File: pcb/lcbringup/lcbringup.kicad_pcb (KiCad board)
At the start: 4 copper layers, 80.8 x 69 mm, 189 parts, among them J1 XILINX_JTAG, J10 SMPM, J11 ARF6-08-S-D-A-K-TR, J12 SMPM, J13 SMPM, J14 SMPM, J15 SMPM, J16 SMPM, J17 SMPM, J18 SMPM, J19 SMPM, J2 CONN_01X10, J20 SMPM, J21 SMPM, J22 SMPM, J23 CONN_IBC_MGMT_HOST, J3 CONN_SFP_HOST, J4 CORTEX_DEBUG_ETM, J5 CONN_01X03, J7 SFP_CAGE, J8 CONN_IBC_MGMT, J9 CONN_ATX12V, M1 SCREWHOLE, M2 SCREWHOLE, M3 SCREWHOLE, M4 SCREWHOLE, U1 XC7A35T-2FGG484C, U10 MUN12AD03-SE, U11 MUN12AD03-SE, U2 STM32H735-UFBGA176-25, U3 ECS-1612MV-250-CN, U4 ECS-1612MV-250-CN, U5 MUN12AD03-SE, U7 AT24MAC402, U8 SIT9121AI-2BF-XXS156.250000G, U9 MUN12AD03-SE

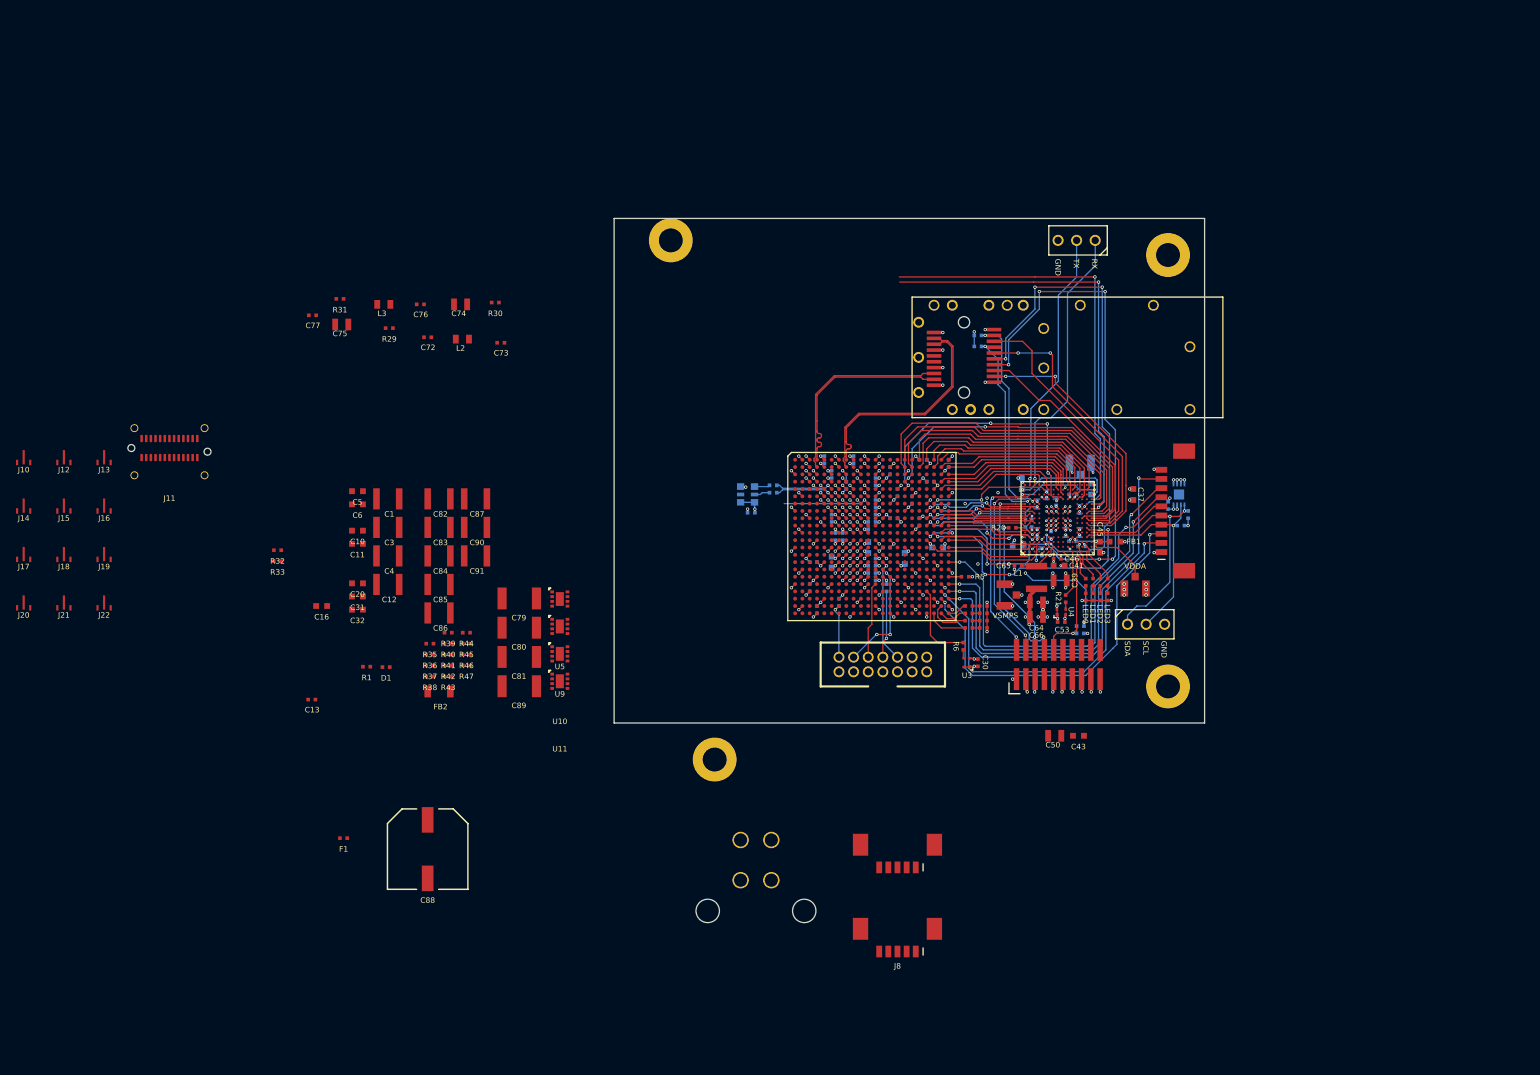
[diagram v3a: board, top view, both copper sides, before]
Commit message: Continued lcbringup layout on ARF6 area
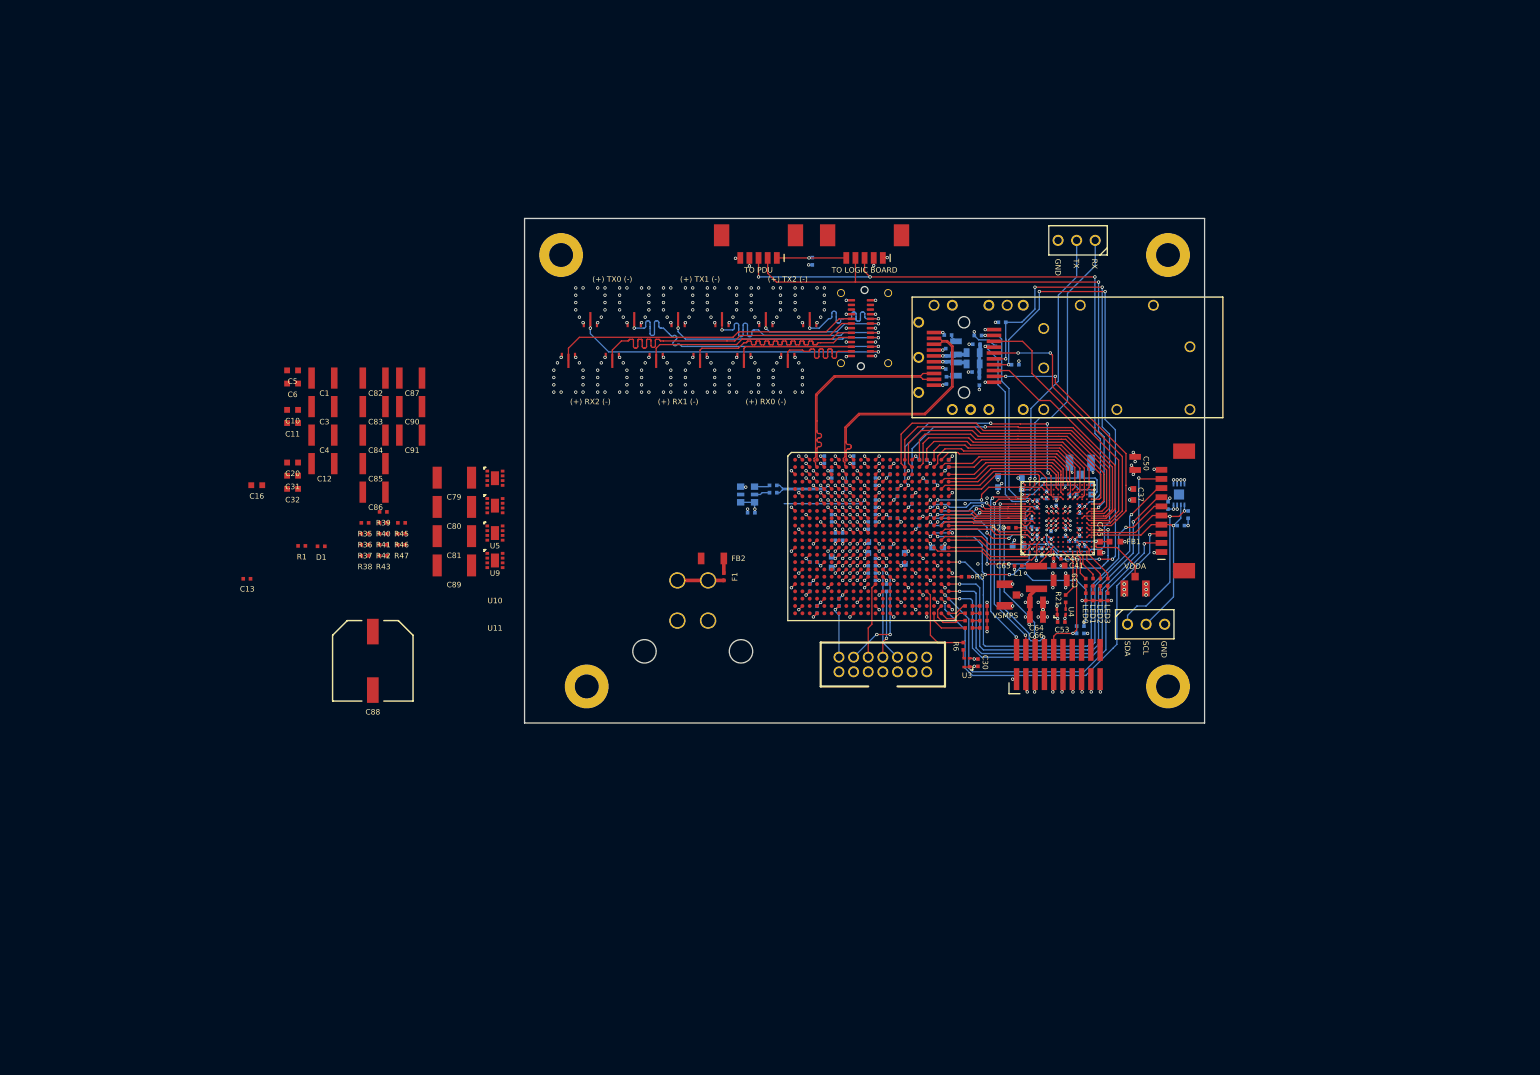
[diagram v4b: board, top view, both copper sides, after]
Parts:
- C43, C72, C73, C74, C75, C76, C77, L2, L3, R29, R30, R31, R32, R33, R44: moved to B.Cu
- moved J17 106.8 mm to (71.0, 45.8), turned to 180 degrees
- moved R33 104.3 mm to (100.3, 38.2), turned to 180 degrees
- moved R32 104.0 mm to (102.1, 44.0)
- moved J16 99.8 mm to (74.0, 35.5)
- moved J15 99.3 mm to (68.0, 35.5)
- moved J14 98.8 mm to (62.0, 35.5)
- moved J8 96.7 mm to (67.0, 29.4)
- moved J11 96.0 mm to (81.0, 39.0), turned to 90 degrees
- moved J18 95.5 mm to (65.0, 45.8), turned to 180 degrees
- moved J20 91.1 mm to (53.0, 45.8), turned to 180 degrees
- moved C77 86.9 mm to (92.6, 44.1), turned to -90 degrees
- moved J19 84.4 mm to (59.0, 45.8), turned to 180 degrees
- moved C75 84.2 mm to (94.0, 44.6), turned to -90 degrees
- moved R31 83.7 mm to (92.7, 46.1), turned to 90 degrees
- moved J23 83.5 mm to (81.5, 29.4)
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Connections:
- J10 pad 2: /ARF6 breakout/GND -> /GND
- J11 pad 1: /ARF6 breakout/GND -> /GND
- J11 pad 13: /ARF6 breakout/GND -> /GND
- J11 pad 14: /ARF6 breakout/GND -> /GND
- J11 pad 19: /ARF6 breakout/GND -> /GND
- J11 pad 2: /ARF6 breakout/GND -> /GND
- J11 pad 20: /ARF6 breakout/GND -> /GND
- J11 pad 25: /ARF6 breakout/GND -> /GND
- J11 pad 26: /ARF6 breakout/GND -> /GND
- J11 pad 27: /ARF6 breakout/GND -> /GND
- J11 pad 7: /ARF6 breakout/GND -> /GND
- J11 pad 8: /ARF6 breakout/GND -> /GND
- J12 pad 2: /ARF6 breakout/GND -> /GND
- J13 pad 2: /ARF6 breakout/GND -> /GND
- J14 pad 2: /ARF6 breakout/GND -> /GND
- J15 pad 2: /ARF6 breakout/GND -> /GND
- J16 pad 2: /ARF6 breakout/GND -> /GND
- J17 pad 2: /ARF6 breakout/GND -> /GND
- J18 pad 2: /ARF6 breakout/GND -> /GND
- J19 pad 2: /ARF6 breakout/GND -> /GND
- J20 pad 2: /ARF6 breakout/GND -> /GND
- J21 pad 2: /ARF6 breakout/GND -> /GND
- J22 pad 2: /ARF6 breakout/GND -> /GND
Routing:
- net /GND: track 745.1 -> 1065.3 mm, vias 195 -> 380
- net /3V3_SB: track 19.2 -> 140.8 mm, vias 4 -> 7
- net /ARF6 breakout/QSGMII_TX0_P: track 0.00 -> 43.5 mm, vias 0 -> 2
- net /ARF6 breakout/QSGMII_TX0_N: track 0.00 -> 43.4 mm, vias 0 -> 2
- net /ARF6 breakout/QSGMII_RX2_N: track 0.00 -> 42.1 mm
- net /ARF6 breakout/QSGMII_RX2_P: track 0.00 -> 42.0 mm
- net /ARF6 breakout/QSGMII_TX1_P: track 0.00 -> 30.7 mm, vias 0 -> 2
- net /ARF6 breakout/QSGMII_TX1_N: track 0.00 -> 30.6 mm, vias 0 -> 2
- net /ARF6 breakout/QSGMII_RX1_N: track 0.00 -> 29.3 mm
- net /ARF6 breakout/QSGMII_RX1_P: track 0.00 -> 29.1 mm
- net /3V3: track 326.1 -> 352.2 mm, vias 71 -> 77
- net /Power supply/SUPER_I2C_SDA: track 60.1 -> 84.9 mm, vias 2 -> 4
- net /Power supply/SUPER_I2C_SCL: track 59.7 -> 83.6 mm
- net /ARF6 breakout/QSGMII_TX2_P: track 0.00 -> 18.4 mm, vias 0 -> 2
- net /ARF6 breakout/QSGMII_TX2_N: track 0.00 -> 18.3 mm, vias 0 -> 2
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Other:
- board size 80.8 x 69 mm -> 93 x 69 mm
- board text added: "(+) RX0 (-)"
- board text added: "(+) RX1 (-)"
- board text added: "(+) RX2 (-)"
- board text added: "(+) TX0 (-)"
- board text added: "(+) TX1 (-)"
- board text added: "(+) TX2 (-)"
- board text added: "TO LOGIC BOARD"
- board text added: "TO PDU"

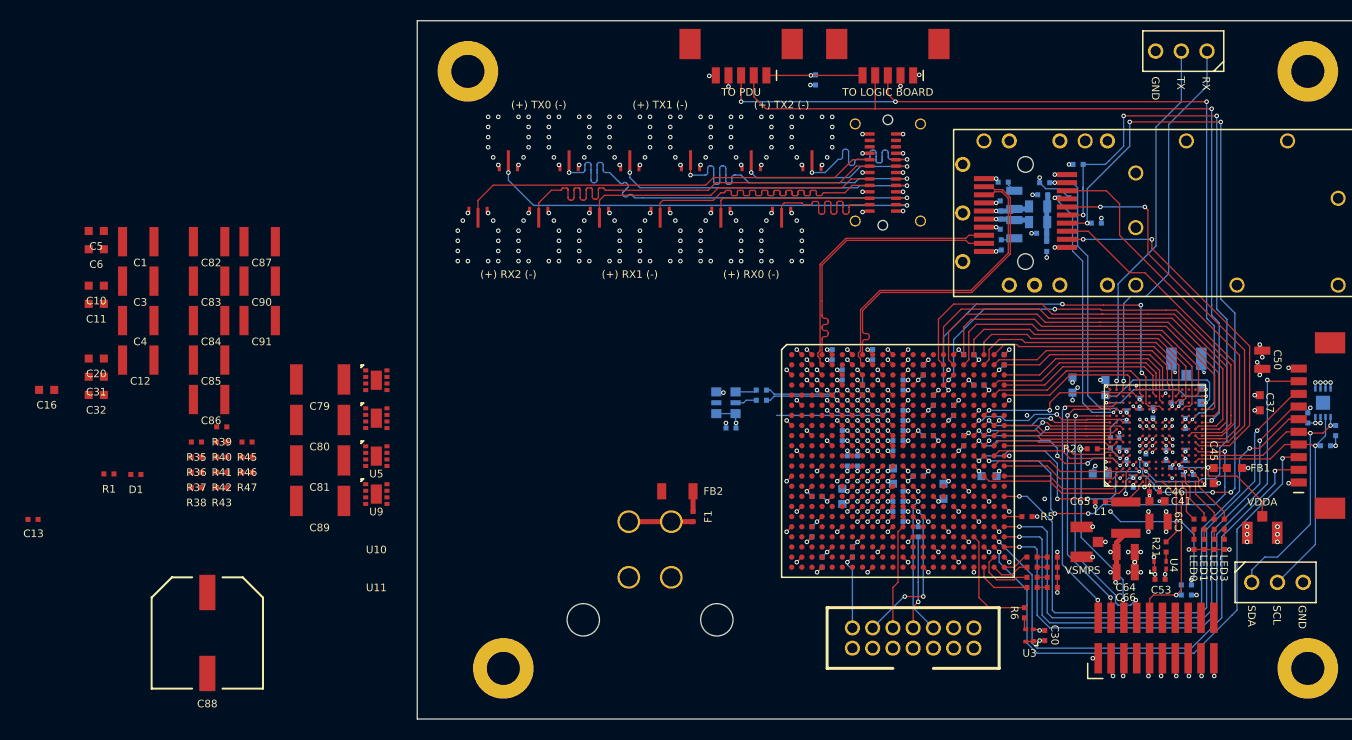
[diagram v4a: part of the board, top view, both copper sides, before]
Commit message: Conitnued lcbringup layout, power supply is now floorplanned
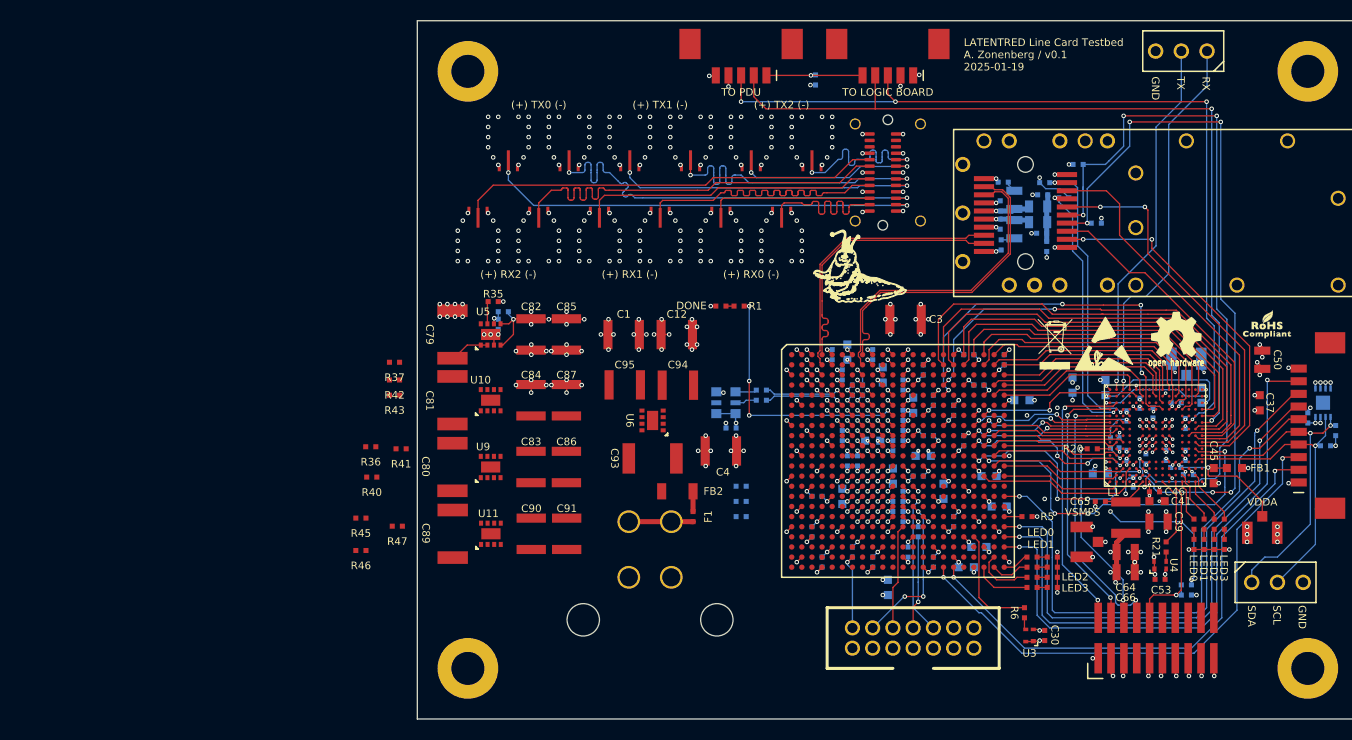
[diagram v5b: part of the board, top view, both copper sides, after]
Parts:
- removed C88: DNP, azonenberg_pcb:CAP_AL_10MM_SMT
- added C100: 0.47 uF, azonenberg_pcb:EIA_0402_CAP_NOSILK, B.Cu at (86.0, 77.5)
- added C101: 0.47 uF, azonenberg_pcb:EIA_0402_CAP_NOSILK, B.Cu at (88.0, 73.5)
- added C93: 22 uF, azonenberg_pcb:EIA_1812_CAP_NOSILK, F.Cu at (58.2, 67.2)
- added C94: 22 uF, azonenberg_pcb:EIA_1210_CAP_NOSILK, F.Cu at (60.8, 60.0)
- added C95: 22 uF, azonenberg_pcb:EIA_1210_CAP_NOSILK, F.Cu at (55.5, 60.0)
- added C96: 4.7 uF, azonenberg_pcb:EIA_0603_CAP_NOSILK, B.Cu at (89.2, 78.0)
- added C97: 4.7 uF, azonenberg_pcb:EIA_0603_CAP_NOSILK, B.Cu at (81.5, 80.0)
- added C98: 0.47 uF, azonenberg_pcb:EIA_0402_CAP_NOSILK, B.Cu at (80.0, 77.5)
- added C99: 0.47 uF, azonenberg_pcb:EIA_0402_CAP_NOSILK, B.Cu at (83.5, 76.5)
- added M5: MECHANICAL, azonenberg_pcb:LONGTHING-1200DPI, F.Cu at (79.3, 48.6)
- added M6: MECHANICAL, azonenberg_pcb:LOGO_ESD_SENSITIVE_7MM, F.Cu at (103.0, 56.0)
- added M7: MECHANICAL, w_logo:Logo_silk_OSHW_6x6mm, F.Cu at (110.0, 55.0)
- added M8: MECHANICAL, w_logo:Logo_silk_ROHS_5x2.8mm, F.Cu at (119.0, 54.0)
- added M9: MECHANICAL, w_logo:Logo_silk_WEEE_3.4x5mm, F.Cu at (98.0, 56.0)
- added R12: 10K, azonenberg_pcb:EIA_0402_RES_NOSILK, B.Cu at (67.0, 70.0)
- added R13: FIXME, azonenberg_pcb:EIA_0402_RES_NOSILK, B.Cu at (67.0, 71.5)
- added R14: FIXME, azonenberg_pcb:EIA_0402_RES_NOSILK, B.Cu at (67.0, 73.0)
- added U6: MUN12AD03-SE, azonenberg_pcb:MODULE_CYNTEC_MUN12AD03-SE, F.Cu at (58.2, 63.5)
- C10, C11, C13, C16, C20, C31, C32, C5, C6, R38, R39: moved to B.Cu
- moved C20 91.6 mm to (94.8, 61.5)
- moved C32 89.9 mm to (92.5, 72.0), turned to 180 degrees
- moved C31 88.8 mm to (90.5, 76.0), turned to 180 degrees
- moved C16 86.9 mm to (85.0, 67.0)
- moved C13 82.0 mm to (78.0, 60.5), turned to 90 degrees
- moved C11 81.3 mm to (84.0, 62.0), turned to -90 degrees
- moved C5 79.0 mm to (81.0, 59.0), turned to 90 degrees
- moved C10 78.2 mm to (80.0, 65.5), turned to 180 degrees
- moved C3 75.9 mm to (83.2, 53.5)
- moved C6 74.9 mm to (77.5, 56.8), turned to 90 degrees
- moved R1 64.4 mm to (66.8, 52.2)
- moved D1 60.2 mm to (65.0, 52.2)
- moved C4 59.0 mm to (65.0, 66.5)
- moved C12 53.3 mm to (60.6, 55.0)
- moved C1 48.8 mm to (55.4, 55.0)
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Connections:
- U1 pad AA17: /3V3 -> /2V5
- U1 pad AB14: /3V3 -> /2V5
- U1 pad AB16: unconnected-(U1C-IO_L2P_T0_13-PadAB16) -> /MDIO and GPIO/MDIO
- U1 pad AB17: unconnected-(U1C-IO_L2N_T0_13-PadAB17) -> /MDIO and GPIO/MDC
- U1 pad V16: /3V3 -> /2V5
- U1 pad W13: /3V3 -> /2V5
- U1 pad W21: /MDIO and GPIO/MDC -> unconnected-(U1D-IO_L7P_T1_D09_14-PadW21)
- U1 pad Y10: /3V3 -> /2V5
- U1 pad Y21: /MDIO and GPIO/MDIO -> unconnected-(U1D-IO_L9P_T1_DQS_14-PadY21)
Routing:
- net /GND: track 1065.3 -> 1186.5 mm, vias 380 -> 421
- net /1V8: track 23.9 -> 97.6 mm, vias 7 -> 19
- net /1V0: track 56.3 -> 124.4 mm, vias 22 -> 38
- net /3V3: track 352.2 -> 409.3 mm
- net /2V5: track 0.00 -> 37.6 mm, vias 0 -> 6
- net Net-(U1A-DONE): track 11.9 -> 25.9 mm, vias 1 -> 4
- net /1V2: track 15.4 -> 22.4 mm
- net /Power supply/12V0: track 0.00 -> 3.99 mm
- net /Power supply/1V8_PGOOD: track 0.00 -> 2.23 mm
- net /Power supply/1V8_FB: track 0.00 -> 1.75 mm, vias 0 -> 1
- net /MDIO and GPIO/MDIO: track 52.3 -> 53.4 mm
- net Net-(D1-A): track 0.00 -> 0.80 mm
- net /MDIO and GPIO/MDC: track 51.3 -> 50.7 mm
- added copper zone on In1.Cu, net /GND
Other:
- board text added: "DONE"
- board text added: "LATENTRED Line Card Testbed A. Zonenberg / v0.1 2025-01-19"

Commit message: Finished initial lcbringup test board, ready for review
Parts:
- J5, TP1: footprint azonenberg_pcb:CONN_HEADER_2.54MM_1x3 -> azonenberg_pcb:CONN_HEADER_2.54MM_1x3_REFLOW
- R13: value FIXME -> 294K
- R14: value FIXME -> 93.1K
- R36, R37, R40, R41, R42, R43, R45, R46, R47: moved to B.Cu
- moved R46 14.5 mm to (43.6, 73.3), turned to 180 degrees
- moved R40 14.0 mm to (44.2, 66.1), turned to 180 degrees
- moved R14 13.9 mm to (58.0, 62.4), turned to 0 degrees
- moved R13 13.8 mm to (56.7, 62.3), turned to -90 degrees
- moved R12 12.9 mm to (55.7, 63.8)
- moved R45 12.5 mm to (41.9, 72.4), turned to 90 degrees
- moved R36 11.5 mm to (41.9, 65.6), turned to 90 degrees
- moved R42 11.0 mm to (43.7, 59.8), turned to 180 degrees
- moved R47 10.7 mm to (43.6, 72.5)
- moved R43 9.85 mm to (42.6, 61.0), turned to -90 degrees
- moved R41 9.63 mm to (43.0, 67.1), turned to -90 degrees
- moved R37 9.25 mm to (41.9, 59.1), turned to 90 degrees
- moved C40 0.10 mm to (112.5, 61.1)
- moved C80 0.10 mm to (38.5, 68.0), turned to 90 degrees
- moved C83 0.10 mm to (46.2, 68.0)
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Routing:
- net /GND: track 1186.5 -> 1343.5 mm, vias 421 -> 491
- net /3V3: track 409.3 -> 504.6 mm, vias 77 -> 87
- net /Power supply/12V0: track 3.99 -> 80.4 mm
- net /1V2: track 22.4 -> 70.2 mm, vias 6 -> 13
- net /2V5: track 37.6 -> 84.2 mm, vias 6 -> 14
- net /1V0: track 124.4 -> 131.2 mm
- net /3V3_SB: track 140.8 -> 143.7 mm
- net /MCU/VSMPS: track 43.4 -> 45.7 mm
- net /Power supply/3V3_FB: track 0.00 -> 1.71 mm, vias 0 -> 1
- net /Power supply/1V0_FB: track 0.00 -> 1.56 mm, vias 0 -> 1
- net /Power supply/2V5_FB: track 0.00 -> 1.48 mm, vias 0 -> 1
- net /Power supply/1V2_FB: track 0.00 -> 1.37 mm, vias 0 -> 1
- net /Power supply/2V5_PGOOD: track 0.00 -> 1.01 mm, vias 0 -> 1
- net /SFP/SFP_RX_P: track 30.8 -> 30.1 mm
- net /SFP/SFP_RX_N: track 30.8 -> 30.0 mm
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- added copper zone on In2.Cu, net /1V0
- added copper zone on In2.Cu, net /1V2
- added copper zone on In2.Cu, net /1V8
- added copper zone on In2.Cu, net /2V5
- added copper zone on In2.Cu, net /3V3
- added copper zone on In2.Cu, net /3V3_SB
- added copper zone on F.Cu, net /GND
- added copper zone on In2.Cu, net /GND
- added copper zone on In2.Cu, net /MCU/VCORE
- added copper zone on In2.Cu, net /MCU/VSMPS
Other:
- board text added: "LATENTRED Line Card Testbed A. Zonenberg / v0.1 2025-01-20"
- board text removed: "LATENTRED Line Card Testbed A. Zonenberg / v0.1 2025-01-19"

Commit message: Finished lcbringup, ready to order
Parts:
- added TP5: GROUNDCLIP, azonenberg_pcb:TESTPOINT_SMT_KEYSTONE_5016, F.Cu at (45.0, 83.0)
- F1: value 3A -> 1A
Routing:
- net /3V3_SB: track 143.7 -> 141.2 mm
- net /MDIO and GPIO/SPI_MISO: track 53.5 -> 52.2 mm
- net /MDIO and GPIO/SPI_SCK: track 52.4 -> 51.3 mm
- net /MDIO and GPIO/SPI_MOSI: track 57.0 -> 56.1 mm
- net /MCU/FMC_NBL1: track 17.4 -> 16.5 mm
- net /MCU/I2C_SDA: track 33.1 -> 32.3 mm
- net /1V8: track 97.2 -> 96.6 mm
- net /GND: vias 491 -> 492
- added copper zone on F.Cu, net /1V0
- added copper zone on F.Cu, net /1V2
- added copper zone on F.Cu, net /1V8
- added copper zone on F.Cu, net /2V5
- added copper zone on F.Cu, net /3V3
- added copper zone on F.Cu, net /Power supply/12V0
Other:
- board text added: "1"
- board text added: "2"
- board text added: "3"
- board text added: "4"
- board text added: "M"
- board text added: "Place UL mark and date code in this area"
- board text added: "S"
